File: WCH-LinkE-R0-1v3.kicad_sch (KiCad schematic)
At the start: 38 parts, among them Q1 DMG1012UW-7, Q2 DMG1012UW-7, SW1 16V 50mA, SW2 16V 50mA, SW3 16V 50mA, U3 CH32V305FBP6

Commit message: Apply suggestions from Petr Dvorak
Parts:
- C18, C19, C20: Comment (none) -> 25V 10uF X5R ±10% 0805
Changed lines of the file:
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@@
+      (effects (font (size 1.27 1.27)) hide)
+    )
+    (property "Comment" "25V 10uF X5R ±10% 0805" (at 95.25 59.69 0)
       (effects (font (size 1.27 1.27)) hide)
     )
@@
       (effects (font (size 1.27 1.27)) hide)
     )
+    (property "Comment" "25V 10uF X5R ±10% 0805" (at 105.41 59.69 0)
+      (effects (font (size 1.27 1.27)) hide)
+    )
     (pin "1")
     (pin "2")
@@
       (effects (font (size 1.27 1.27)) hide)
     )
+    (property "Comment" "25V 10uF X5R ±10% 0805" (at 100.33 59.69 0)
+      (effects (font (size 1.27 1.27)) hide)
+    )

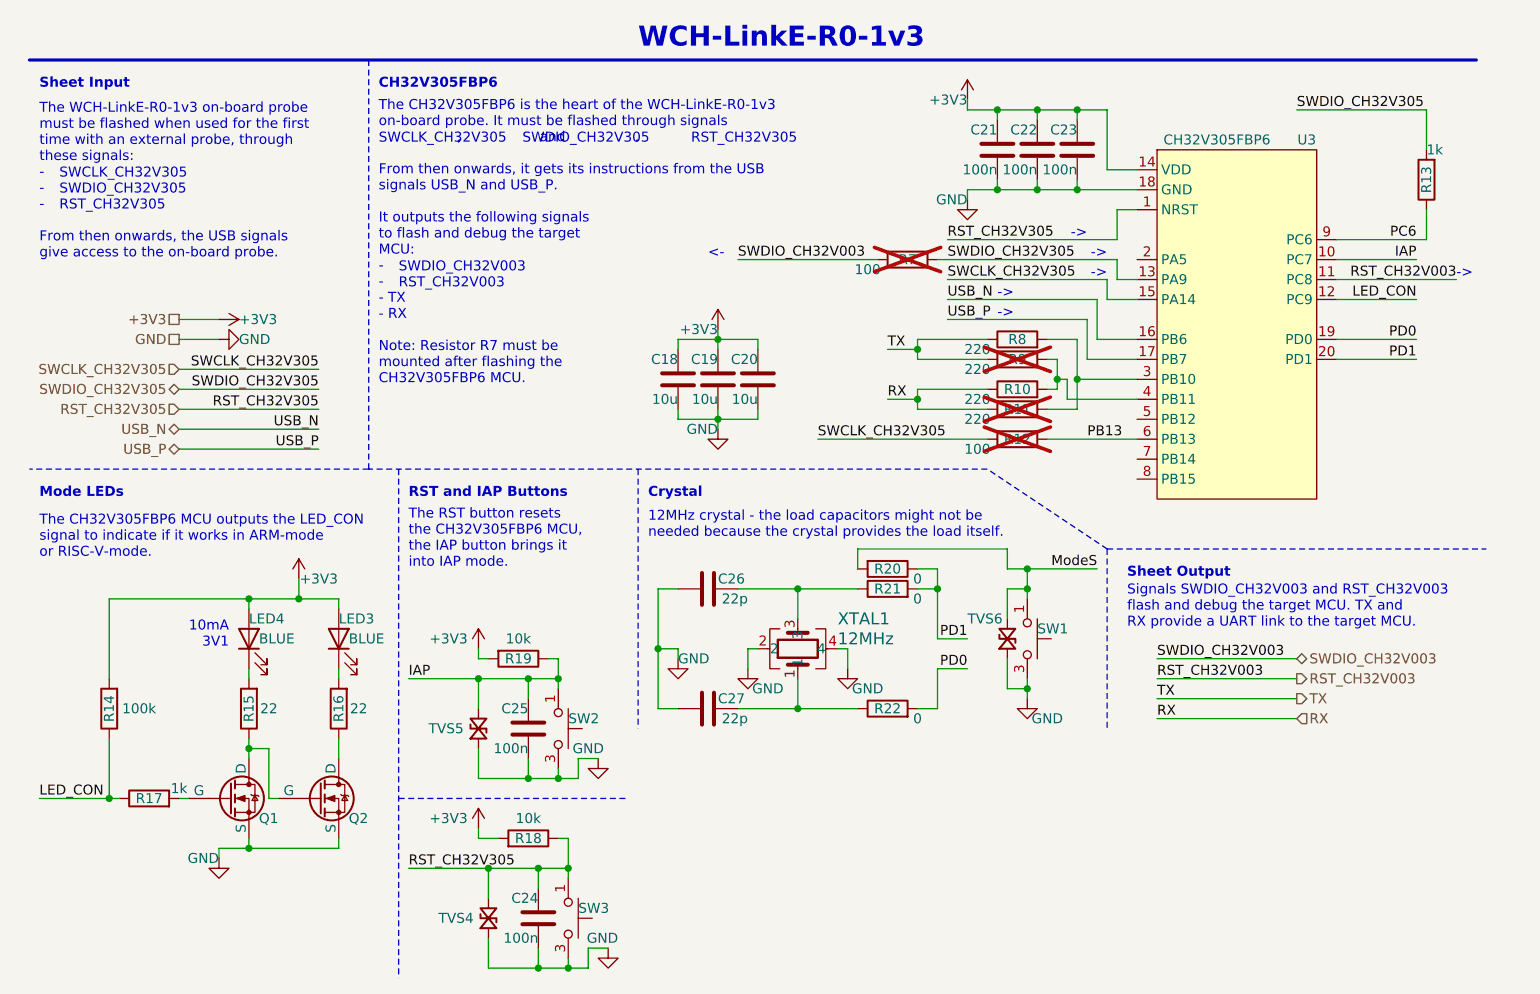
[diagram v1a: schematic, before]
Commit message: Rename capacitors
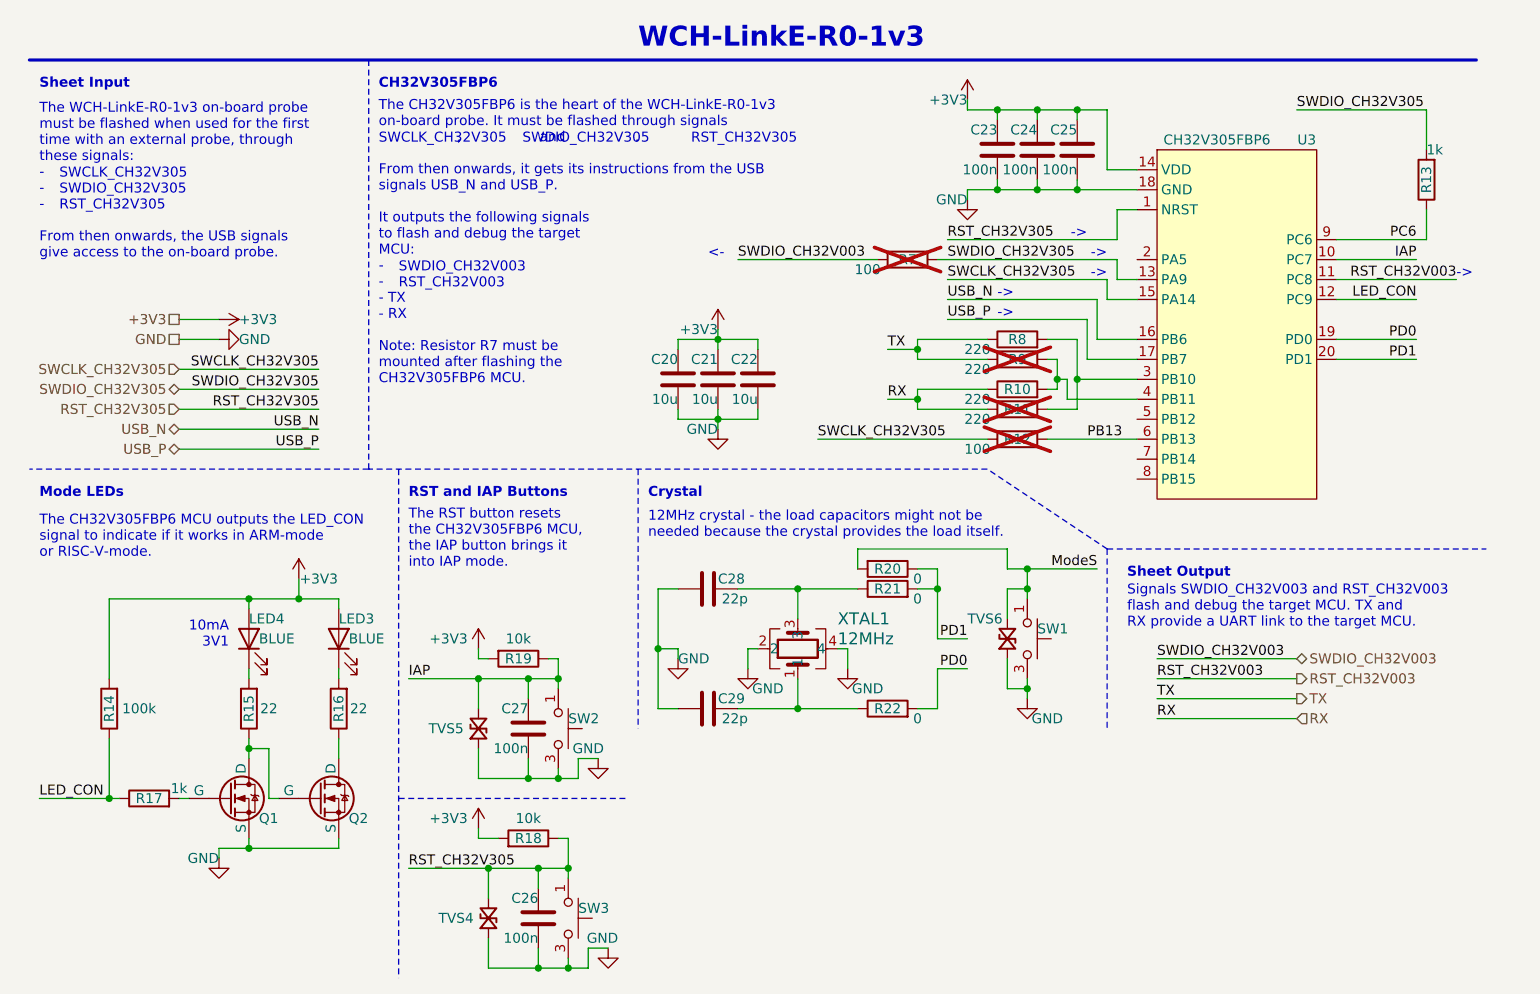
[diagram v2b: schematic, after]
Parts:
- C23: renamed from C21; Comment (none) -> 16V 100nF X7R ±10% 0402
- C24: renamed from C22; Comment (none) -> 16V 100nF X7R ±10% 0402
- C25: renamed from C23; Comment (none) -> 16V 100nF X7R ±10% 0402
- C26: renamed from C24; Comment (none) -> 16V 100nF X7R ±10% 0402
- C27: renamed from C25; Comment (none) -> 16V 100nF X7R ±10% 0402
- C28: renamed from C26; Comment (none) -> 50V 22pF C0G ±5% 0402
- C29: renamed from C27; Comment (none) -> 50V 22pF C0G ±5% 0402
- renumbered C18 to C20, C19 to C21, C20 to C22

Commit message: Update parts
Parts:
- removed SW1, SW2, SW3: 16V 50mA, Tiny_Scarab:SW_Tactile_SPST_NO_Straight_ALPSALPINE_SKRP, symbol Tiny_Scarab:SW_SKRPASE010
- added SW1, SW2: 12V 50mA, Tiny_Scarab:SW_Tactile_SPST_NO_Straight_Korean-Hroparts_K2-1109SP-A4SA-04, symbol Tiny_Scarab:SW_K2-1109SP-A4SA-04
- added SW3: 12V 50mA, Tiny_Scarab:SW_Tactile_SPST_NO_Straight_Korean-Hroparts_K2-1109SP-I4SA-04, symbol Tiny_Scarab:SW_K2-1109SP-I4SA-04
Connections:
- net GND: now also SW1.3, SW1.4, SW2.3, SW2.4, SW3.3, SW3.4
- net IAP: now also SW2.1, SW2.2
- net ModeS: now also SW1.1, SW1.2
- net RST_CH32V305: now also SW3.1, SW3.2

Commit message: Work on Graphic Overlay Membrane
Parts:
- removed SW3: 12V 50mA, Tiny_Scarab:SW_Tactile_SPST_NO_Straight_Korean-Hroparts_K2-1109SP-I4SA-04, symbol Tiny_Scarab:SW_K2-1109SP-I4SA-04
- added SW3: 12V 50mA, Tiny_Scarab:SW_Tactile_SPST_NO_Straight_Korean-Hroparts_K2-1109SP-A4SA-04, symbol Tiny_Scarab:SW_K2-1109SP-A4SA-04
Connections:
- net GND: now also SW3.3, SW3.4
- net RST_CH32V305: now also SW3.1, SW3.2
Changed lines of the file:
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@@
+    )
+  )
+  (symbol (lib_id "Tiny_Scarab:SW_K2-1109SP-A4SA-04") (at 80.01 104.14 270) (unit 1)
+    (in_bom yes) (on_board yes) (dnp no)
+    (property "Reference" "SW2" (at 81.28 102.87 90)
+      (effects (font (size 1.27 1.27)) (justify left))
+    )
+    (property "Value" "12V 50mA" (at 105.41 104.14 0)
+      (effects (font (size 1.27 1.27)) hide)
+    )
+    (property "Footprint" "Tiny_Scarab:SW_Tactile_SPST_NO_Straight_Korean-Hroparts_K2-1109SP-A4SA-04" (at 107.95 104.14 0)
+      (effects (font (size 1.27 1.27)) hide)
+    )
+    (property "Datasheet" "" (at 102.87 104.14 0)
+      (effects (font (size 1.27 1.27)) hide)
+    )
+    (property "Manufacturer" "Korean Hroparts Elec" (at 100.33 104.14 0)
+      (effects (font (size 1.27 1.27)) hide)
+    )
+    (property "MPN" "K2-1109SP-A4SA-04" (at 97.79 104.14 0)
+      (effects (font (size 1.27 1.27)) hide)
+    )
+    (property "JLCPCB Part #" "C92581" (at 95.25 104.14 0)
+      (effects (font (size 1.27 1.27)) hide)
+    )
+    (property "DigiKey" "" (at 92.71 104.14 0)
+      (effects (font (size 1.27 1.27)) hide)
+    )
+    (property "Farnell" "" (at 90.17 104.14 0)
+      (effects (font (size 1.27 1.27)) hide)
+    )
+    (property "Mouser" "" (at 87.63 104.14 0)
+      (effects (font (size 1.27 1.27)) hide)
+    )
+    (pin "1")
+    (pin "3")
+    (pin "2")
+    (pin "4")
+    (instances
+      (project "tiny-scarab"
+        (path "/156c5422-ee07-49a4-8263-a2dbd26b90bd/90393844-9805-4207-88e8-abd4029c5b43"
+          (reference "SW2") (unit 1)
+        )
+      )
     )
   )
@@
     )
   )
+  (symbol (lib_id "Tiny_Scarab:SW_K2-1109SP-A4SA-04") (at 81.28 128.27 270) (unit 1)
+    (in_bom yes) (on_board yes) (dnp no)
+    (property "Reference" "SW3" (at 82.55 127 90)
+      (effects (font (size 1.27 1.27)) (justify left))
+    )
+    (property "Value" "12V 50mA" (at 106.68 128.27 0)
+      (effects (font (size 1.27 1.27)) hide)
+    )
+    (property "Footprint" "Tiny_Scarab:SW_Tactile_SPST_NO_Straight_Korean-Hroparts_K2-1109SP-A4SA-04" (at 109.22 128.27 0)
+      (effects (font (size 1.27 1.27)) hide)
+    )
+    (property "Datasheet" "" (at 104.14 128.27 0)
+      (effects (font (size 1.27 1.27)) hide)
+    )
+    (property "Manufacturer" "Korean Hroparts Elec" (at 101.6 128.27 0)
+      (effects (font (size 1.27 1.27)) hide)
+    )
+    (property "MPN" "K2-1109SP-A4SA-04" (at 99.06 128.27 0)
+      (effects (font (size 1.27 1.27)) hide)
+    )
+    (property "JLCPCB Part #" "C92581" (at 96.52 128.27 0)
+      (effects (font (size 1.27 1.27)) hide)
+    )
+    (property "DigiKey" "" (at 93.98 128.27 0)
+      (effects (font (size 1.27 1.27)) hide)
+    )
+    (property "Farnell" "" (at 91.44 128.27 0)
+      (effects (font (size 1.27 1.27)) hide)
+    )
+    (property "Mouser" "" (at 88.9 128.27 0)
+      (effects (font (size 1.27 1.27)) hide)
+    )
+    (pin "1")
+    (pin "3")
+    (pin "2")
+    (pin "4")
+    (instances
+      (project "tiny-scarab"
+        (path "/156c5422-ee07-49a4-8263-a2dbd26b90bd/90393844-9805-4207-88e8-abd4029c5b43"
+          (reference "SW3") (unit 1)
+        )
+      )
+    )
+  )
   (symbol (lib_id "Device:C") (at 77.47 128.27 0) (mirror y) (unit 1)
     (in_bom yes) (on_board yes) (dnp no)
@@
     )
   )
-  (symbol (lib_id "Tiny_Scarab:SW_K2-1109SP-I4SA-04") (at 81.28 128.27 270) (unit 1)
-    (in_bom yes) (on_board yes) (dnp no)
-    (property "Reference" "SW3" (at 82.55 127 90)
-      (effects (font (size 1.27 1.27)) (justify left))
-    )
-    (property "Value" "12V 50mA" (at 106.68 128.27 0)
-      (effects (font (size 1.27 1.27)) hide)
-    )
-    (property "Footprint" "Tiny_Scarab:SW_Tactile_SPST_NO_Straight_Korean-Hroparts_K2-1109SP-I4SA-04" (at 109.22 128.27 0)
-      (effects (font (size 1.27 1.27)) hide)
-    )
-    (property "Datasheet" "" (at 104.14 128.27 0)
-      (effects (font (size 1.27 1.27)) hide)
-    )
-    (property "Manufacturer" "Korean Hroparts Elec" (at 101.6 128.27 0)
-      (effects (font (size 1.27 1.27)) hide)
-    )
-    (property "MPN" "K2-1109SP-I4SA-04" (at 99.06 128.27 0)
-      (effects (font (size 1.27 1.27)) hide)
-    )
-    (property "JLCPCB Part #" "C146695" (at 96.52 128.27 0)
-      (effects (font (size 1.27 1.27)) hide)
-    )
-    (property "DigiKey" "" (at 93.98 128.27 0)
-      (effects (font (size 1.27 1.27)) hide)
-    )
-    (property "Farnell" "" (at 91.44 128.27 0)
-      (effects (font (size 1.27 1.27)) hide)
-    )
-    (property "Mouser" "" (at 88.9 128.27 0)
-      (effects (font (size 1.27 1.27)) hide)
-    )
-    (pin "2")
-    (pin "4")
-    (pin "1")
-    (pin "3")
-    (instances
-      (project "tiny-scarab"
-        (path "/156c5422-ee07-49a4-8263-a2dbd26b90bd/90393844-9805-4207-88e8-abd4029c5b43"
-          (reference "SW3") (unit 1)
-        )
-      )
-    )
-  )
   (symbol (lib_id "power:GND") (at 139.7 100.33 0) (unit 1)
     (in_bom yes) (on_board yes) (dnp no)
@@
         )
       )
-    )
-  )
-  (symbol (lib_id "Tiny_Scarab:SW_K2-1109SP-A4SA-04") (at 80.01 104.14 270) (unit 1)
-    (in_bom yes) (on_board yes) (dnp no)
-    (property "Reference" "SW2" (at 81.28 102.87 90)
-      (effects (font (size 1.27 1.27)) (justify left))
-    )
-    (property "Value" "12V 50mA" (at 105.41 104.14 0)
-      (effects (font (size 1.27 1.27)) hide)
-    )
-    (property "Footprint" "Tiny_Scarab:SW_Tactile_SPST_NO_Straight_Korean-Hroparts_K2-1109SP-A4SA-04" (at 107.95 104.14 0)
-      (effects (font (size 1.27 1.27)) hide)
-    )
-    (property "Datasheet" "" (at 102.87 104.14 0)
-      (effects (font (size 1.27 1.27)) hide)
-    )
-    (property "Manufacturer" "Korean Hroparts Elec" (at 100.33 104.14 0)
-      (effects (font (size 1.27 1.27)) hide)
-    )
-    (property "MPN" "K2-1109SP-A4SA-04" (at 97.79 104.14 0)
-      (effects (font (size 1.27 1.27)) hide)
-    )
-    (property "JLCPCB Part #" "C92581" (at 95.25 104.14 0)
-      (effects (font (size 1.27 1.27)) hide)
-    )
-    (property "DigiKey" "" (at 92.71 104.14 0)
-      (effects (font (size 1.27 1.27)) hide)
-    )
-    (property "Farnell" "" (at 90.17 104.14 0)
-      (effects (font (size 1.27 1.27)) hide)
-    )
-    (property "Mouser" "" (at 87.63 104.14 0)
-      (effects (font (size 1.27 1.27)) hide)
-    )
-    (pin "1")
-    (pin "3")
-    (pin "2")
-    (pin "4")
-    (instances
-      (project "tiny-scarab"
-        (path "/156c5422-ee07-49a4-8263-a2dbd26b90bd/90393844-9805-4207-88e8-abd4029c5b43"
-          (reference "SW2") (unit 1)
-        )
-      )
